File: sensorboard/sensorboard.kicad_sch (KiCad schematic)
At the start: 66 parts, among them J10 Conn_01x02_Male, J11 Conn_01x05_Male, J9 Conn_01x02_Male, Q1 MMDT2222A, U1 ESP32-PICO-D4, U2 LTC4411, U3 TPS61092RSAR

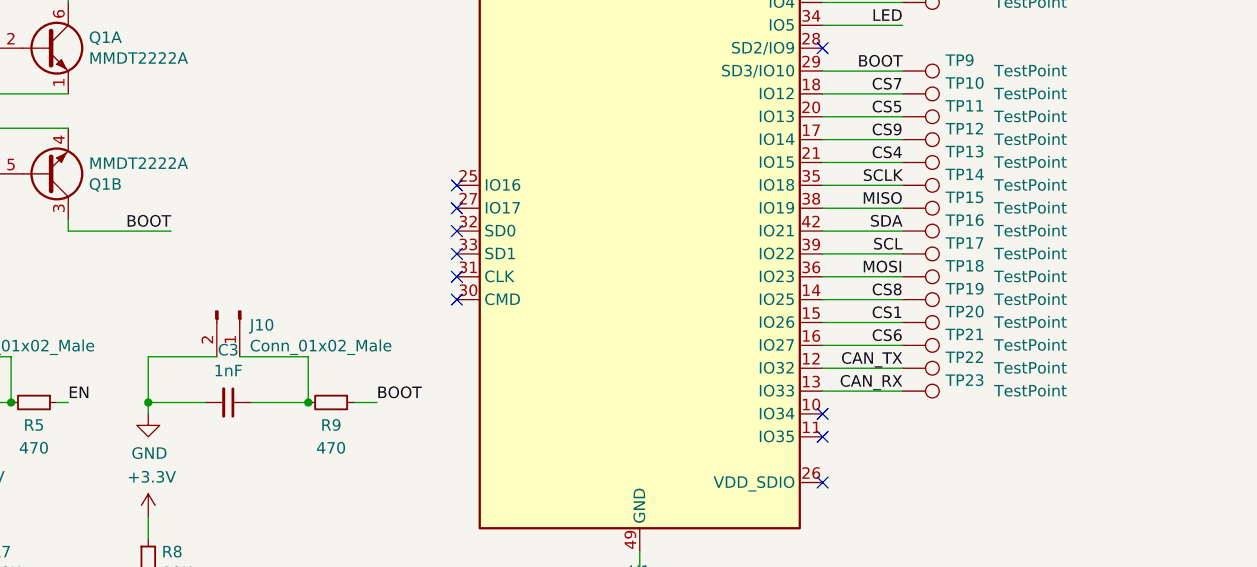
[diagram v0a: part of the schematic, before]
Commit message: Integrated in USB and CAN
CAN_TX and CAN_RX are moved
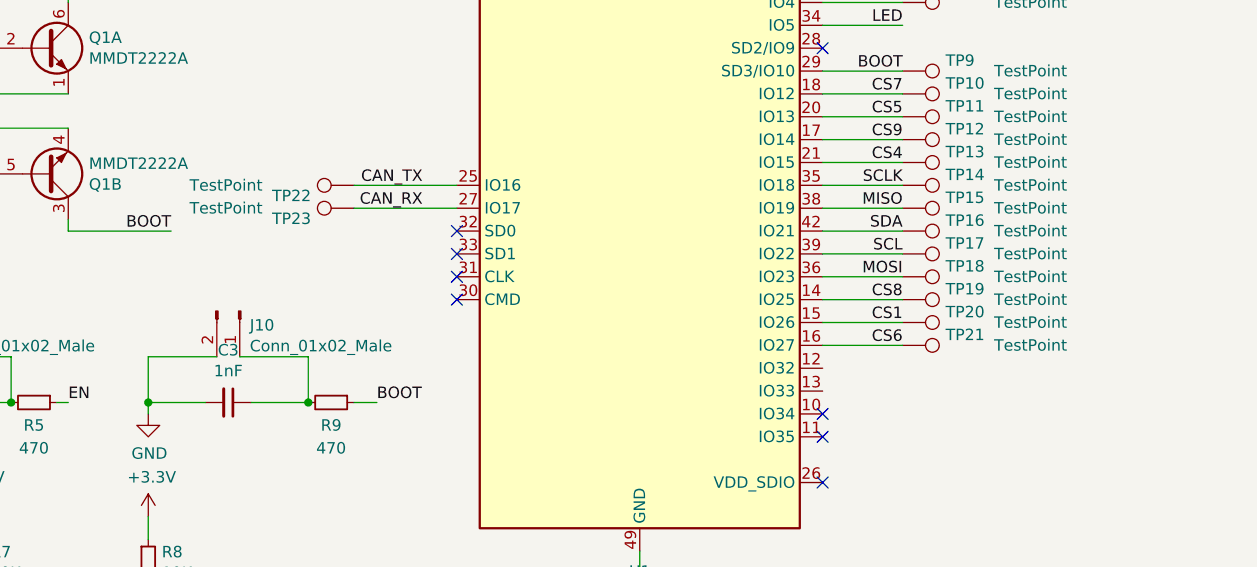
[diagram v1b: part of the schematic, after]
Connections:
- net CAN_RX: now also U1.27 (IO17); no longer U1.13 (IO33)
- net CAN_TX: now also U1.25 (IO16); no longer U1.12 (IO32)
- no-connect marks 37 -> 35
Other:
- moved on the sheet: TP22, TP23
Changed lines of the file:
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@@
   (no_connect (at 175.26 104.14))
   (no_connect (at 83.82 151.13))
-  (no_connect (at 83.82 148.59))
   (no_connect (at 276.86 59.69))
   (no_connect (at 83.82 120.65))
@@
   (no_connect (at 248.92 76.2))
   (no_connect (at 248.92 57.15))
-  (no_connect (at 83.82 146.05))
   (no_connect (at 248.92 40.64))
   (no_connect (at 276.86 92.71))
@@
     (stroke (width 0) (type default) (color 0 0 0 0))
   )
+  (wire (pts (xy 72.39 146.05) (xy 83.82 146.05))
+    (stroke (width 0) (type default) (color 0 0 0 0))
+  )
   (wire (pts (xy 49.53 165.1) (xy 49.53 170.18))
     (stroke (width 0) (type default) (color 0 0 0 0))
@@
     (stroke (width 0) (type default) (color 0 0 0 0))
   )
+  (wire (pts (xy 72.39 148.59) (xy 83.82 148.59))
+    (stroke (width 0) (type default) (color 0 0 0 0))
+  )
   (wire (pts (xy 16.51 165.1) (xy 24.13 165.1))
     (stroke (width 0) (type default) (color 0 0 0 0))
@@
     (stroke (width 0) (type default) (color 0 0 0 0))
   )
-  (wire (pts (xy 124.46 166.37) (xy 133.35 166.37))
-    (stroke (width 0) (type default) (color 0 0 0 0))
-  )
   (polyline (pts (xy 158.75 54.61) (xy 158.75 16.51))
     (stroke (width 0) (type default) (color 0 0 0 0))
@@
   )
   (wire (pts (xy 102.87 92.71) (xy 102.87 95.25))
-    (stroke (width 0) (type default) (color 0 0 0 0))
-  )
-  (wire (pts (xy 124.46 168.91) (xy 133.35 168.91))
     (stroke (width 0) (type default) (color 0 0 0 0))
   )
@@
     (effects (font (size 1.27 1.27)) (justify left bottom))
   )
-  (label "CAN_TX" (at 133.35 166.37 180)
+  (label "CAN_TX" (at 80.01 146.05 180)
     (effects (font (size 1.27 1.27)) (justify right bottom))
   )
@@
     (effects (font (size 1.27 1.27)) (justify left bottom))
   )
-  (label "CAN_RX" (at 133.35 168.91 180)
+  (label "CAN_RX" (at 80.01 148.59 180)
     (effects (font (size 1.27 1.27)) (justify right bottom))
   )
@@
     (pin "1")
   )
-  (symbol (lib_id "Connector:TestPoint") (at 133.35 168.91 270) (unit 1)
-    (in_bom yes) (on_board yes)
-    (property "Reference" "TP23" (id 0) (at 138.1252 167.7416 90)
+  (symbol (lib_id "Connector:TestPoint") (at 72.39 148.59 90) (unit 1)
+    (in_bom yes) (on_board yes)
+    (property "Reference" "TP23" (id 0) (at 67.6148 149.7584 90)
       (effects (font (size 1.27 1.27)) (justify left))
     )
-    (property "Value" "TestPoint" (id 1) (at 143.51 168.91 90)
+    (property "Value" "TestPoint" (id 1) (at 62.23 148.59 90)
       (effects (font (size 1.27 1.27)) (justify left))
     )
-    (property "Footprint" "TestPoint:TestPoint_Pad_D1.0mm" (id 2) (at 133.35 173.99 0)
-      (effects (font (size 1.27 1.27)) hide)
-    )
-    (property "Datasheet" "~" (id 3) (at 133.35 173.99 0)
-      (effects (font (size 1.27 1.27)) hide)
-    )
-    (pin "1")
-  )
-  (symbol (lib_id "Connector:TestPoint") (at 133.35 166.37 270) (unit 1)
-    (in_bom yes) (on_board yes)
-    (property "Reference" "TP22" (id 0) (at 138.1252 165.2016 90)
+    (property "Footprint" "TestPoint:TestPoint_Pad_D1.0mm" (id 2) (at 72.39 143.51 0)
+      (effects (font (size 1.27 1.27)) hide)
+    )
+    (property "Datasheet" "~" (id 3) (at 72.39 143.51 0)
+      (effects (font (size 1.27 1.27)) hide)
+    )
+    (pin "1")
+  )
+  (symbol (lib_id "Connector:TestPoint") (at 72.39 146.05 90) (unit 1)
+    (in_bom yes) (on_board yes)
+    (property "Reference" "TP22" (id 0) (at 67.6148 147.2184 90)
       (effects (font (size 1.27 1.27)) (justify left))
     )
-    (property "Value" "TestPoint" (id 1) (at 143.51 166.37 90)
+    (property "Value" "TestPoint" (id 1) (at 62.23 146.05 90)
       (effects (font (size 1.27 1.27)) (justify left))
     )
-    (property "Footprint" "TestPoint:TestPoint_Pad_D1.0mm" (id 2) (at 133.35 171.45 0)
-      (effects (font (size 1.27 1.27)) hide)
-    )
-    (property "Datasheet" "~" (id 3) (at 133.35 171.45 0)
-      (effects (font (size 1.27 1.27)) hide)
-    )
+    (property "Footprint" "TestPoint:TestPoint_Pad_D1.0mm" (id 2) (at 72.39 140.97 0)
+      (effects (font (size 1.27 1.27)) hide)
+    )
+    (property "Datasheet" "~" (id 3) (at 72.39 140.97 0)
+      (effects (font (size 1.27 1.27)) hide)
+    )

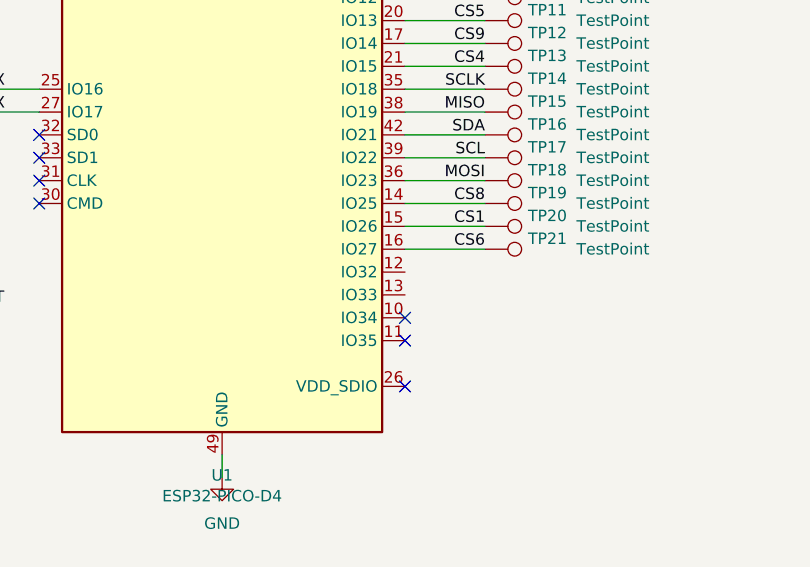
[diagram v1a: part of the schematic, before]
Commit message: moved the U14 component and added component
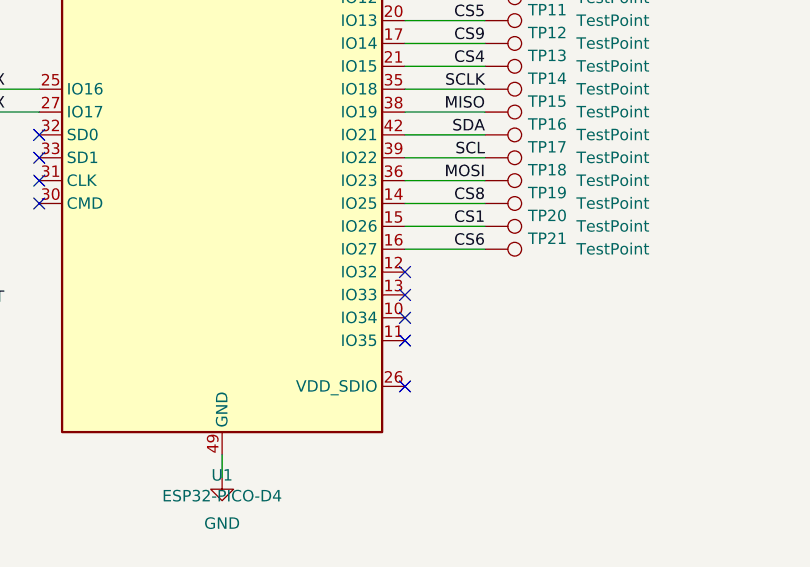
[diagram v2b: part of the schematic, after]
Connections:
- no-connect marks 35 -> 37
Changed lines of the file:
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@@
   (no_connect (at 83.82 151.13))
   (no_connect (at 276.86 59.69))
+  (no_connect (at 124.46 166.37))
+  (no_connect (at 124.46 168.91))
   (no_connect (at 83.82 120.65))
   (no_connect (at 83.82 123.19))

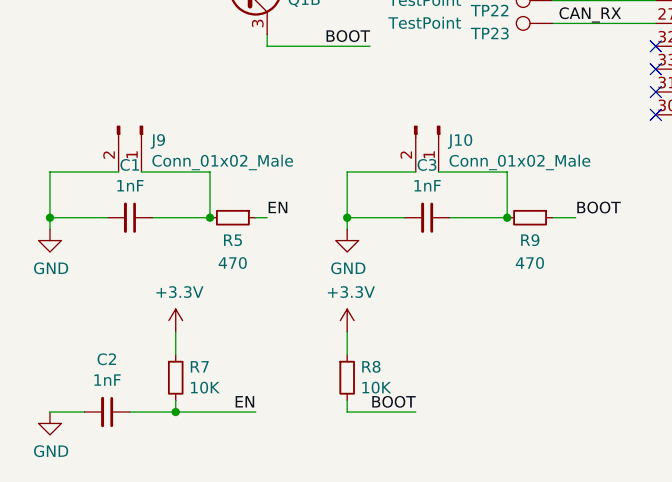
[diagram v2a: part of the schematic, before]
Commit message: connectors and changed capacitor values
capacitors for the connectors to 0.1uf
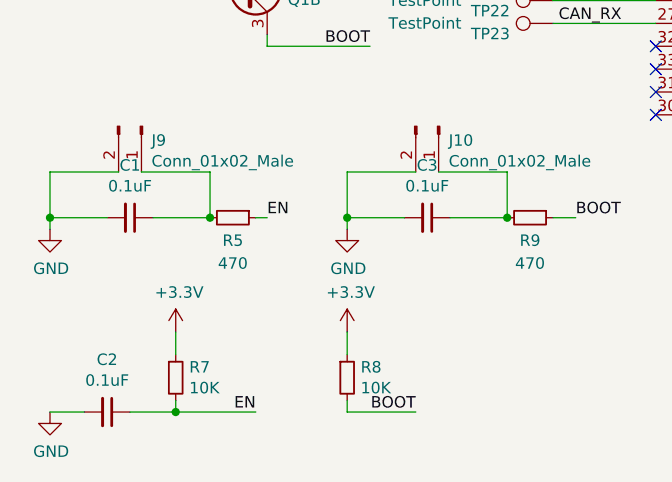
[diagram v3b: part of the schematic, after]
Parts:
- C1, C2, C3: value 1nF -> 0.1uF
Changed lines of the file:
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@@
     (in_bom yes) (on_board yes)
     (property "Reference" "C2" (id 0) (at 22.86 185.9534 90))
-    (property "Value" "1nF" (id 1) (at 22.86 188.2648 90))
+    (property "Value" "0.1uF" (id 1) (at 22.86 188.2648 90))
     (property "Footprint" "Capacitor_SMD:C_0603_1608Metric" (id 2) (at 22.86 191.77 0)
       (effects (font (size 1.27 1.27)) hide)
@@
     (in_bom yes) (on_board yes)
     (property "Reference" "C3" (id 0) (at 58.42 164.3634 90))
-    (property "Value" "1nF" (id 1) (at 58.42 166.6748 90))
+    (property "Value" "0.1uF" (id 1) (at 58.42 166.6748 90))
     (property "Footprint" "Capacitor_SMD:C_0603_1608Metric" (id 2) (at 58.42 170.18 0)
       (effects (font (size 1.27 1.27)) hide)
@@
     (in_bom yes) (on_board yes)
     (property "Reference" "C1" (id 0) (at 25.4 164.3634 90))
-    (property "Value" "1nF" (id 1) (at 25.4 166.6748 90))
+    (property "Value" "0.1uF" (id 1) (at 25.4 166.6748 90))
     (property "Footprint" "Capacitor_SMD:C_0603_1608Metric" (id 2) (at 25.4 170.18 0)
       (effects (font (size 1.27 1.27)) hide)
@@
     )
     (path "/00000000-0000-0000-0000-00005dabbfe7"
-      (reference "C1") (unit 1) (value "1nF") (footprint "Capacitor_SMD:C_0603_1608Metric")
+      (reference "C1") (unit 1) (value "0.1uF") (footprint "Capacitor_SMD:C_0603_1608Metric")
     )
     (path "/00000000-0000-0000-0000-00005da70d8a"
-      (reference "C2") (unit 1) (value "1nF") (footprint "Capacitor_SMD:C_0603_1608Metric")
+      (reference "C2") (unit 1) (value "0.1uF") (footprint "Capacitor_SMD:C_0603_1608Metric")
     )
     (path "/00000000-0000-0000-0000-00005dab5946"
-      (reference "C3") (unit 1) (value "1nF") (footprint "Capacitor_SMD:C_0603_1608Metric")
+      (reference "C3") (unit 1) (value "0.1uF") (footprint "Capacitor_SMD:C_0603_1608Metric")
     )
     (path "/00000000-0000-0000-0000-0000619dacb2"

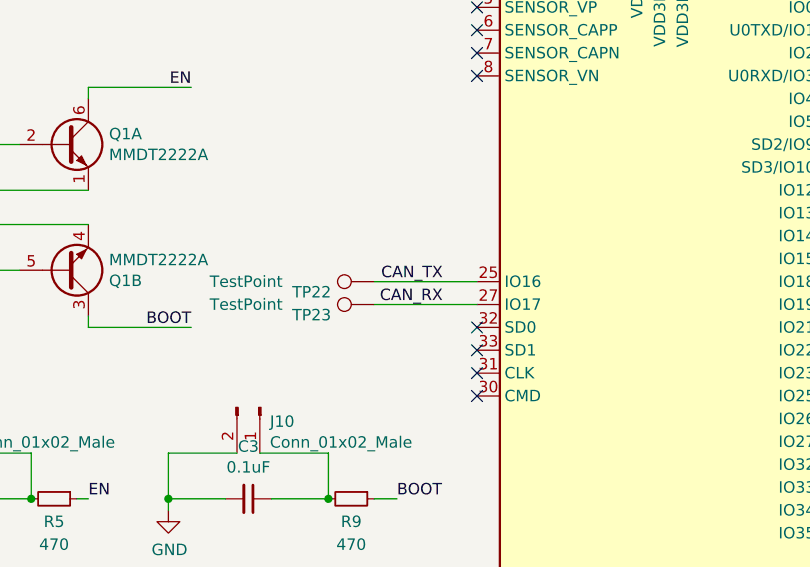
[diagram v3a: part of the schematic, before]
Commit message: rearrange CAN, USB port and new copies
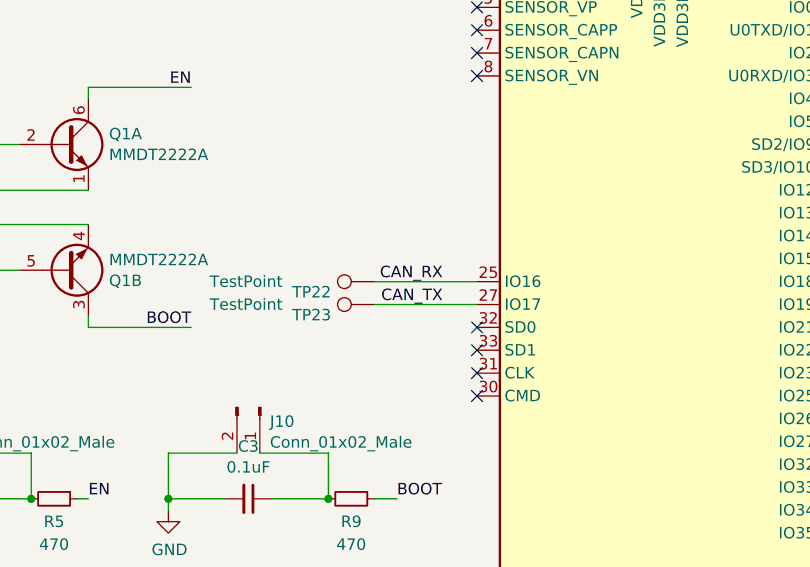
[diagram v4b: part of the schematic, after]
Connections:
- net CAN_RX: now also TP22.1, U1.25 (IO16); no longer TP23.1, U1.27 (IO17)
- net CAN_TX: now also TP23.1, U1.27 (IO17); no longer TP22.1, U1.25 (IO16)
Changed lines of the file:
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@@
     (effects (font (size 1.27 1.27)) (justify left bottom))
   )
-  (label "CAN_TX" (at 80.01 146.05 180)
+  (label "CAN_TX" (at 80.01 148.59 180)
     (effects (font (size 1.27 1.27)) (justify right bottom))
   )
@@
     (effects (font (size 1.27 1.27)) (justify left bottom))
   )
-  (label "CAN_RX" (at 80.01 148.59 180)
+  (label "CAN_RX" (at 80.01 146.05 180)
     (effects (font (size 1.27 1.27)) (justify right bottom))
   )
